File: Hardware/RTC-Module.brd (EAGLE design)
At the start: 25.4 x 25.4 mm, 21 parts, among them U1 RV-4162-C7

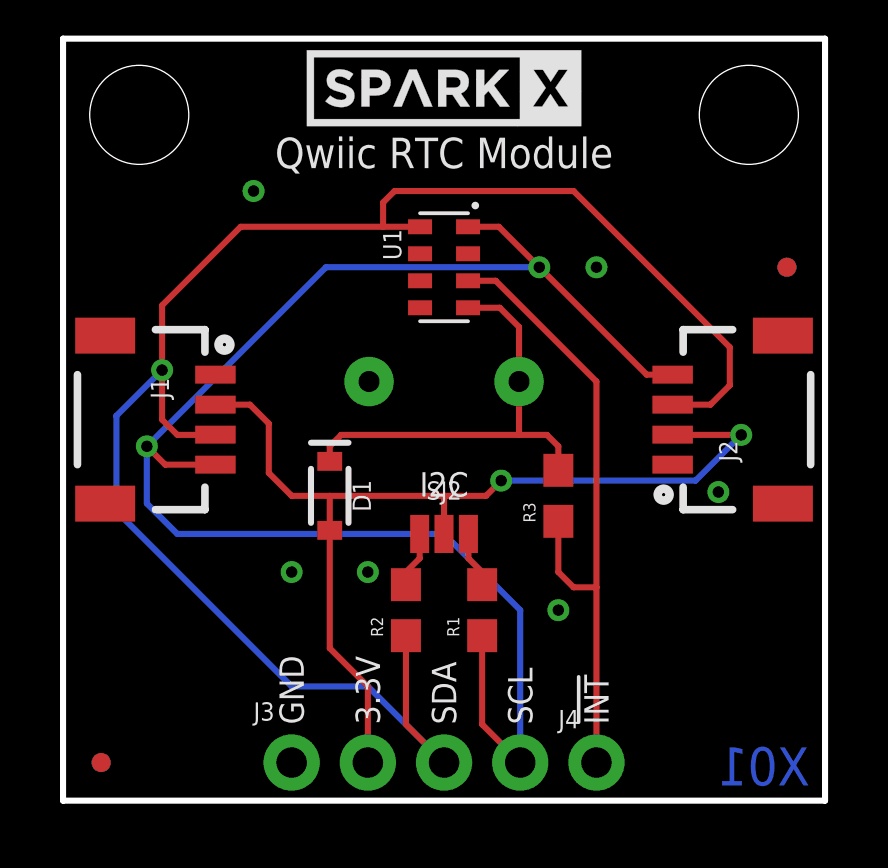
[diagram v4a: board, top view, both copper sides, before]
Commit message: updated to RV-1805
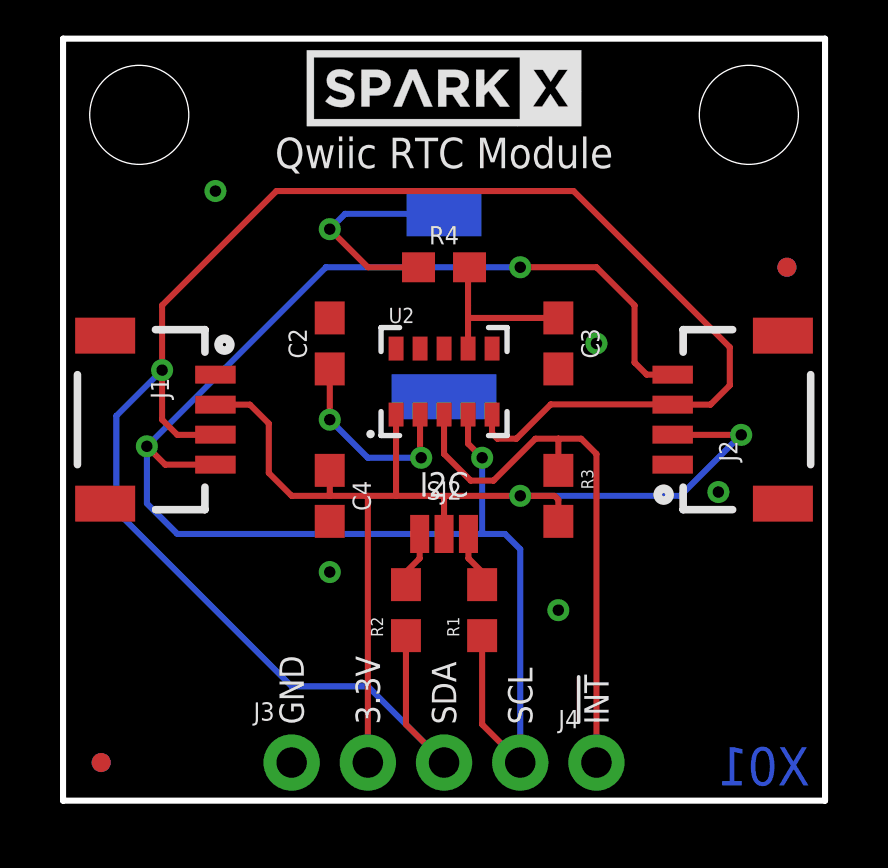
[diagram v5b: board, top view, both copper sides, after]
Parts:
- removed D1: 0.5A/40V/420mV, SparkFun-DiscreteSemi:SOD-323
- removed U1: RV-4162-C7, SparkFun-Clocks:RV-4162-C7-SMT
- added C2: 47pF, SparkFun-Capacitors:0603
- added C3, C4: 10nF, SparkFun-Capacitors:0603
- added R4: 1.5k, SparkFun-Resistors:0603
- added U2: RV-1805, SparkFun-Clocks:RV-1805
- C1: value 1F-EDLC -> 70MF-SUPERCAP; device SparkFun-Capacitors:CAP-RADIAL-5MM-21.5MM -> SparkFun-Capacitors:DSK-RADIAL-4.8MM
- moved C1 2.54 mm to (12.7, 16.5)
- turned R3 to 270 degrees
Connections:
- removed net CLKOUT: U1.2
- removed net VBATT: C1.+, D1.C, R3.2, U1.5
- new net N$3: C1.+, R4.1
- new net N$4: C2.1, U2.2
- new net VBACKUP: C3.1, R4.2, U2.7
- net !INT: now also U2.3; no longer U1.6
- net 3.3V: now also C4.1, R3.2, U2.1; no longer D1.A
- net GND: now also C2.2, C3.2, C4.2, U2.6, U2.8, U2.9; no longer U1.3
- net SCL: now also U2.4; no longer U1.8
- net SDA: now also U2.5; no longer U1.1
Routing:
- net VBATT: track 14.8 -> 0.00 mm
- net N$3: track 0.00 -> 7.51 mm, vias 0 -> 1
- net N$4: track 0.00 -> 6.72 mm, vias 0 -> 2
- net VBACKUP: track 0.00 -> 5.74 mm
- net SDA: track 58.1 -> 63.6 mm
- net 3.3V: track 33.6 -> 38.6 mm
- net SCL: track 52.6 -> 56.2 mm, vias 2 -> 3
- net !INT: track 21.5 -> 18.9 mm

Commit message: updated cap value
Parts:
- C1: value 70MF-SUPERCAP -> 220MF-SUPERCAP
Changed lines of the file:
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@@
 </element>
 <element name="J4" library="SparkFun-Connectors" package="1X01_NO_SILK" value="" x="17.78" y="1.27"/>
-<element name="C1" library="SparkFun-Capacitors" package="DSK-RADIAL-4.8MM" value="70MF-SUPERCAP" x="12.7" y="16.51" rot="MR0">
+<element name="C1" library="SparkFun-Capacitors" package="DSK-RADIAL-4.8MM" value="220MF-SUPERCAP" x="12.7" y="16.51" rot="MR0">
 <attribute name="PROD_ID" value="CAP-13907" x="12.7" y="16.51" size="1.778" layer="28" rot="MR0" display="off"/>
 </element>

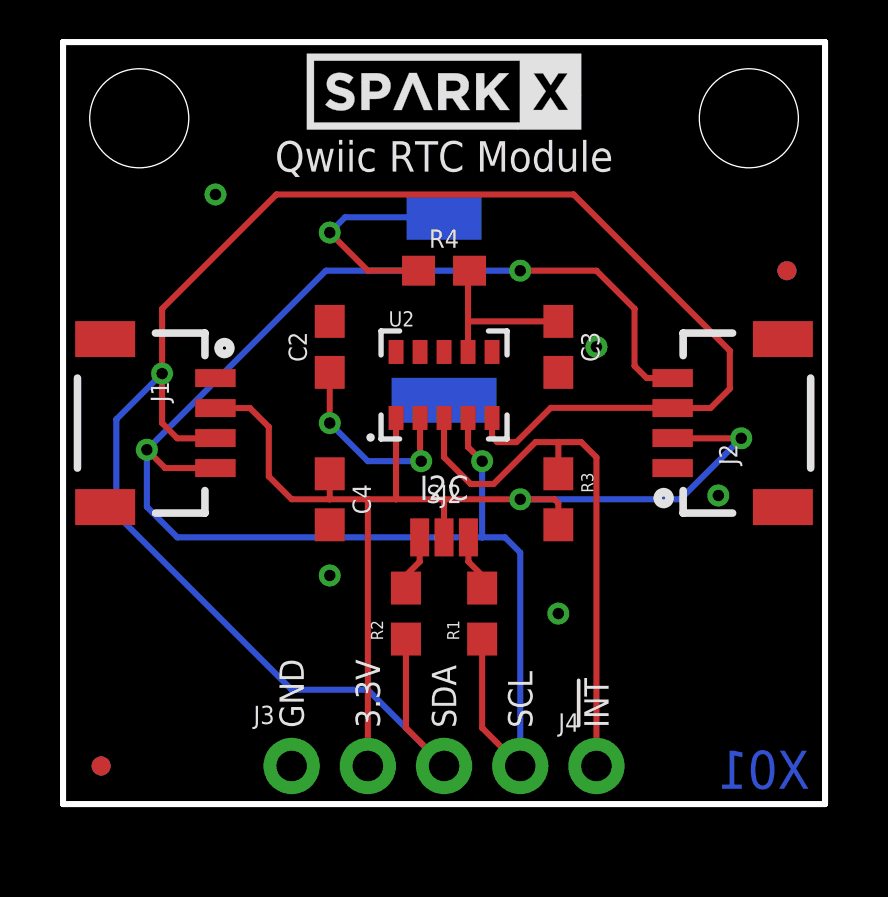
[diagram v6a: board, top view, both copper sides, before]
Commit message: Updated cap footprint, broke out rest of pins
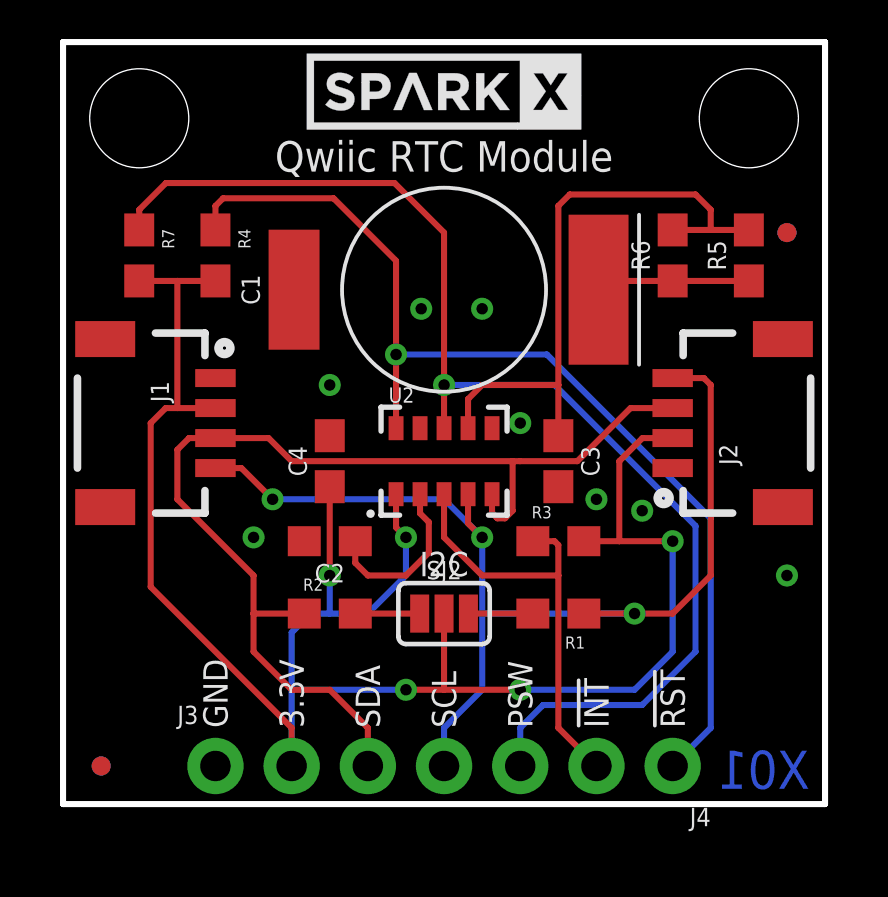
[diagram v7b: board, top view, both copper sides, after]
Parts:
- added R5, R6: 2.55k, SparkFun-Resistors:0603
- added R7: 4.7k, SparkFun-Resistors:0603@1
- C1: value 220MF-SUPERCAP -> .22F-SUPERCAP
- J4: device SparkFun-Connectors:1X01_NO_SILK -> SparkFun-Connectors:1X03_NO_SILK
- R4: value 1.5k -> 4.7k; device SparkFun-Resistors:0603 -> SparkFun-Resistors:0603@1
- SJ2: value JUMPER-SMT_3_2-NC_PASTE_NO-SILK -> JUMPER-SMT_3_2-NC_PASTE_SILK; device SparkFun-Jumpers:SMT-JUMPER_3_2-NC_PASTE_NO-SILK -> SparkFun-Jumpers:SMT-JUMPER_3_2-NC_PASTE_SILK
- moved R4 7.64 mm to (5.08, 18.3), turned to 270 degrees
- moved C2 6.48 mm to (8.89, 8.76), turned to 180 degrees
- moved C3 3.81 mm to (16.5, 11.4)
- moved LOGO1 2.84 mm to (2.54, 4.19)
- moved R1 2.54 mm to (16.5, 6.35), turned to 180 degrees
- moved SJ2 2.54 mm to (12.7, 6.35)
- moved U2 2.54 mm to (12.7, 11.4)
- moved J3 2.54 mm to (5.08, 1.27)
- moved U$3 2.54 mm to (3.81, 6.86)
- moved J4 2.54 mm to (20.3, 1.27), turned to 180 degrees
- moved R2 2.54 mm to (8.89, 6.35), turned to 0 degrees
- moved R3 1.40 mm to (16.5, 8.76), turned to 0 degrees
- moved C4 1.27 mm to (8.89, 11.4), turned to 90 degrees
- moved FD1 1.27 mm to (24.1, 19.1)
- moved FD2 1.27 mm to (24.1, 19.1)
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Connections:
- removed net N$3: C1.+, R4.1
- new net !RST: J4.1, R4.1, U2.10
- new net N$5: C1.+, R5.1, R6.1
- new net PSW: J4.3, R7.1, U2.8
- net !INT: now also J4.2; no longer J4.1
- net 3.3V: now also R4.2, R7.2
- net GND: no longer U2.8
- net VBACKUP: now also R5.2, R6.2; no longer R4.2
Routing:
- net PSW: track 0.00 -> 41.1 mm, vias 0 -> 1
- net !RST: track 0.00 -> 34.9 mm, vias 0 -> 1
- net 3.3V: track 38.6 -> 65.8 mm, vias 2 -> 5
- net SDA: track 63.6 -> 36.5 mm, vias 1 -> 0
- net SCL: track 56.2 -> 37.2 mm
- net VBACKUP: track 5.74 -> 20.6 mm
- net N$3: track 7.51 -> 0.00 mm, vias 1 -> 0
- net N$5: track 0.00 -> 7.19 mm
- net !INT: track 18.9 -> 14.6 mm
- net N$4: track 6.72 -> 5.73 mm, vias 2 -> 0
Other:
- board text added: "!RST"
- board text added: "PSW"

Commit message: Moved via
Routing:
- net 3.3V: track 65.8 -> 65.1 mm
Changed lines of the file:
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@@
 <wire x1="3.81" y1="13.2" x2="3.81" y2="17.438" width="0.2032" layer="1"/>
 <wire x1="12.7" y1="6.35" x2="12.7" y2="3.81" width="0.2032" layer="1"/>
-<wire x1="12.7" y1="3.81" x2="15.24" y2="3.81" width="0.2032" layer="1"/>
-<via x="15.24" y="3.81" extent="1-16" drill="0.381"/>
-<wire x1="15.24" y1="3.81" x2="19.05" y2="3.81" width="0.2032" layer="16"/>
-<wire x1="19.05" y1="3.81" x2="20.32" y2="5.08" width="0.2032" layer="16"/>
-<wire x1="20.32" y1="5.08" x2="20.32" y2="8.763" width="0.2032" layer="16"/>
+<via x="15.24" y="5.08" extent="1-16" drill="0.381"/>
 <wire x1="17.36" y1="8.763" x2="18.542" y2="8.763" width="0.2032" layer="1"/>
 <via x="20.32" y="8.763" extent="1-16" drill="0.381"/>
@@
 <wire x1="7.62" y1="2.54" x2="2.921" y2="7.239" width="0.2032" layer="1"/>
 <wire x1="2.921" y1="7.239" x2="2.921" y2="12.7" width="0.2032" layer="1"/>
+<wire x1="20.32" y1="6.35" x2="20.32" y2="8.763" width="0.2032" layer="16"/>
+<wire x1="20.32" y1="6.35" x2="19.05" y2="5.08" width="0.2032" layer="16"/>
+<wire x1="19.05" y1="5.08" x2="15.24" y2="5.08" width="0.2032" layer="16"/>
+<wire x1="12.7" y1="3.81" x2="13.97" y2="3.81" width="0.2032" layer="1"/>
+<wire x1="13.97" y1="3.81" x2="15.24" y2="5.08" width="0.2032" layer="1"/>
 </signal>
 <signal name="!INT">
